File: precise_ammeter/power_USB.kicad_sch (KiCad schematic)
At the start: 21 parts, among them J3 USB4110GFA, J5 XT30_Male, U10 TPS7A2450DBVR, U7 TPS7A2433DBVR, U8 TPS7A2450DBVR, U9 LMC7660

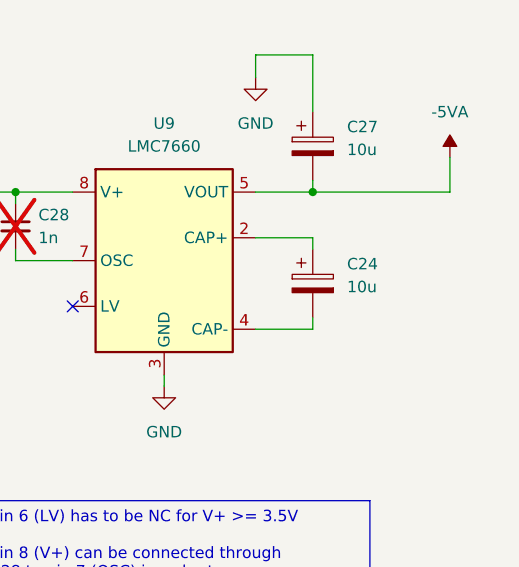
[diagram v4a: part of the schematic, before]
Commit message: adding 1 more 10u cap at voltage inverter
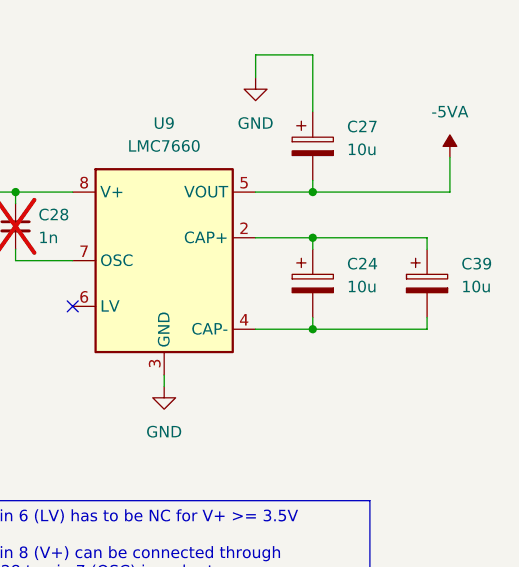
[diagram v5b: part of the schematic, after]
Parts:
- added C39: 10u, Capacitor_SMD:CP_Elec_4x5.4, symbol Device:C_Polarized
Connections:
- net at C24.1, U9.2 (CAP+): now also C39.1
- net at C24.2, U9.4 (CAP-): now also C39.2
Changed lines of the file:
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@@
 	)
 	(junction
+		(at 257.81 115.57)
+		(diameter 0)
+		(color 0 0 0 0)
+	)
+	(junction
 		(at 81.28 127)
 		(diameter 0)
@@
 	)
 	(junction
+		(at 257.81 125.73)
+		(diameter 0)
+		(color 0 0 0 0)
+	)
+	(junction
 		(at 100.33 181.61)
 		(diameter 0)
@@
 	(wire
 		(pts
+			(xy 270.51 115.57) (xy 257.81 115.57)
+		)
+		(stroke
+			(width 0)
+			(type default)
+		)
+	)
+	(wire
+		(pts
 			(xy 85.09 114.3) (xy 81.28 114.3)
 		)
@@
 	(wire
 		(pts
+			(xy 270.51 116.84) (xy 270.51 115.57)
+		)
+		(stroke
+			(width 0)
+			(type default)
+		)
+	)
+	(wire
+		(pts
 			(xy 210.82 46.99) (xy 207.01 46.99)
 		)
@@
 	(wire
 		(pts
-			(xy 194.31 40.64) (xy 194.31 44.45)
+			(xy 257.81 115.57) (xy 257.81 116.84)
 		)
 		(stroke
@@
 	(wire
 		(pts
-			(xy 110.49 116.84) (xy 110.49 119.38)
+			(xy 194.31 40.64) (xy 194.31 44.45)
 		)
 		(stroke
@@
 	(wire
 		(pts
-			(xy 163.83 110.49) (xy 167.64 110.49)
+			(xy 110.49 116.84) (xy 110.49 119.38)
 		)
 		(stroke
@@
 	(wire
 		(pts
-			(xy 251.46 115.57) (xy 257.81 115.57)
+			(xy 163.83 110.49) (xy 167.64 110.49)
 		)
 		(stroke
@@
 	(wire
 		(pts
-			(xy 81.28 45.72) (xy 85.09 45.72)
+			(xy 251.46 115.57) (xy 257.81 115.57)
 		)
 		(stroke
@@
 	(wire
 		(pts
-			(xy 106.68 55.88) (xy 114.3 55.88)
+			(xy 81.28 45.72) (xy 85.09 45.72)
 		)
 		(stroke
@@
 	(wire
 		(pts
-			(xy 257.81 124.46) (xy 257.81 125.73)
+			(xy 106.68 55.88) (xy 114.3 55.88)
 		)
 		(stroke
@@
 	(wire
 		(pts
-			(xy 257.81 115.57) (xy 257.81 116.84)
+			(xy 257.81 124.46) (xy 257.81 125.73)
 		)
 		(stroke
@@
 	(wire
 		(pts
+			(xy 270.51 124.46) (xy 270.51 125.73)
+		)
+		(stroke
+			(width 0)
+			(type default)
+		)
+	)
+	(wire
+		(pts
 			(xy 81.28 116.84) (xy 81.28 121.92)
 		)
@@
 	(wire
 		(pts
+			(xy 257.81 125.73) (xy 270.51 125.73)
+		)
+		(stroke
+			(width 0)
+			(type default)
+		)
+	)
+	(wire
+		(pts
 			(xy 60.96 181.61) (xy 60.96 176.53)
 		)
@@
 					(unit 1)
 				)
+			)
+		)
+	)
+	(symbol
+		(lib_id "Device:C_Polarized")
+		(at 270.51 120.65 0)
+		(unit 1)
+		(exclude_from_sim no)
+		(in_bom yes)
+		(on_board yes)
+		(dnp no)
+		(fields_autoplaced yes)
+		(property "Reference" "C39"
+			(at 274.32 118.4909 0)
+			(effects
+				(font
+					(size 1.27 1.27)
+				)
+				(justify left)
+			)
+		)
+		(property "Value" "10u"
+			(at 274.32 121.0309 0)
+			(effects
+				(font
+					(size 1.27 1.27)
+				)
+				(justify left)
+			)
+		)
+		(property "Footprint" "Capacitor_SMD:CP_Elec_4x5.4"
+			(at 271.4752 124.46 0)
+			(effects
+				(font
+					(size 1.27 1.27)
+				)
+				(hide yes)
+			)
+		)
+		(property "Datasheet" "~"
+			(at 270.51 120.65 0)
+			(effects
+				(font
+					(size 1.27 1.27)
+				)
+				(hide yes)
+			)
+		)
+		(property "Description" "Polarized capacitor"
+			(at 270.51 120.65 0)
+			(effects
+				(font
+					(size 1.27 1.27)
+				)
+				(hide yes)
+			)
+		)
+		(property "Product link" "EDH106M025S9BAA"
+			(at 270.51 120.65 0)
+			(effects
+				(font
+					(size 1.27 1.27)
+				)
+				(hide yes)
+			)
+		)
+		(pin "2"
+		)
+		(pin "1"
+		)
+		(instances
+			(project "precise_ammeter"
+				(path "/7da3b652-85ac-4caa-8d8d-9cad461e9c85/9e6d6147-95e6-4ef0-a238-5628802dd2a2"
+					(reference "C39")
+					(unit 1)
+				)

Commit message: added step model for xt30
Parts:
- J5: footprint Connector_AMASS:AMASS_XT30UPB-M_1x02_P5.0mm_Vertical -> xt30:AMASS_XT30UPB-M_1x02_P5.0mm_Vertical
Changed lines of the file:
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@@
 			)
 		)
-		(property "Footprint" "Connector_AMASS:AMASS_XT30UPB-M_1x02_P5.0mm_Vertical"
+		(property "Footprint" "xt30:AMASS_XT30UPB-M_1x02_P5.0mm_Vertical"
 			(at 33.02 64.77 0)
 			(effects

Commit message: layout started
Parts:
- U10, U8: footprint TPS7A2450DBVR:SOT_50DBVR -> TPS7A2433DBVR:SOT23_DBV_TEX
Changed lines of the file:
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@@
 			)
 		)
-		(property "Footprint" "TPS7A2450DBVR:SOT_50DBVR"
+		(property "Footprint" "TPS7A2433DBVR:SOT23_DBV_TEX"
 			(at 194.818 97.536 0)
 			(effects
@@
 			)
 		)
-		(property "Footprint" "TPS7A2450DBVR:SOT_50DBVR"
+		(property "Footprint" "TPS7A2433DBVR:SOT23_DBV_TEX"
 			(at 225.298 31.496 0)
 			(effects

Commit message: placement finished
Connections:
- net GND: now also J5.1 (Pin_1); no longer J5.2 (Pin_2)
- net VBUS: now also J5.2 (Pin_2); no longer J5.1 (Pin_1)
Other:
- moved on the sheet: J5
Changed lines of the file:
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@@
 	(wire
 		(pts
+			(xy 38.1 71.12) (xy 31.75 71.12)
+		)
+		(stroke
+			(width 0)
+			(type default)
+		)
+	)
+	(wire
+		(pts
 			(xy 257.81 110.49) (xy 273.05 110.49)
 		)
@@
 	(wire
 		(pts
-			(xy 38.1 67.31) (xy 41.91 67.31)
+			(xy 106.68 57.15) (xy 106.68 55.88)
 		)
 		(stroke
@@
 	(wire
 		(pts
-			(xy 106.68 57.15) (xy 106.68 55.88)
+			(xy 232.41 55.88) (xy 232.41 54.61)
 		)
 		(stroke
@@
 	(wire
 		(pts
-			(xy 232.41 55.88) (xy 232.41 54.61)
+			(xy 110.49 121.92) (xy 130.81 121.92)
 		)
 		(stroke
@@
 	(wire
 		(pts
-			(xy 110.49 121.92) (xy 130.81 121.92)
+			(xy 60.96 181.61) (xy 64.77 181.61)
 		)
 		(stroke
@@
 	(wire
 		(pts
-			(xy 60.96 181.61) (xy 64.77 181.61)
+			(xy 114.3 45.72) (xy 114.3 46.99)
 		)
 		(stroke
@@
 	(wire
 		(pts
-			(xy 114.3 45.72) (xy 114.3 46.99)
+			(xy 167.64 111.76) (xy 167.64 110.49)
 		)
 		(stroke
@@
 	(wire
 		(pts
-			(xy 167.64 111.76) (xy 167.64 110.49)
+			(xy 224.79 118.11) (xy 224.79 116.84)
 		)
 		(stroke
@@
 	(wire
 		(pts
-			(xy 41.91 64.77) (xy 41.91 62.23)
+			(xy 257.81 115.57) (xy 257.81 116.84)
 		)
 		(stroke
@@
 	(wire
 		(pts
-			(xy 224.79 118.11) (xy 224.79 116.84)
+			(xy 194.31 40.64) (xy 194.31 44.45)
 		)
 		(stroke
@@
 	(wire
 		(pts
-			(xy 257.81 115.57) (xy 257.81 116.84)
+			(xy 110.49 116.84) (xy 110.49 119.38)
 		)
 		(stroke
@@
 	(wire
 		(pts
-			(xy 194.31 40.64) (xy 194.31 44.45)
+			(xy 163.83 110.49) (xy 167.64 110.49)
 		)
 		(stroke
@@
 	(wire
 		(pts
-			(xy 110.49 116.84) (xy 110.49 119.38)
+			(xy 38.1 68.58) (xy 31.75 68.58)
 		)
 		(stroke
@@
 	(wire
 		(pts
-			(xy 163.83 110.49) (xy 167.64 110.49)
+			(xy 251.46 115.57) (xy 257.81 115.57)
 		)
 		(stroke
@@
 	(wire
 		(pts
-			(xy 251.46 115.57) (xy 257.81 115.57)
+			(xy 31.75 71.12) (xy 31.75 73.66)
 		)
 		(stroke
@@
 	(wire
 		(pts
-			(xy 81.28 121.92) (xy 85.09 121.92)
+			(xy 31.75 68.58) (xy 31.75 66.04)
 		)
 		(stroke
@@
 	(wire
 		(pts
-			(xy 194.31 44.45) (xy 198.12 44.45)
+			(xy 81.28 121.92) (xy 85.09 121.92)
 		)
 		(stroke
@@
 	(wire
 		(pts
-			(xy 85.09 129.54) (xy 81.28 129.54)
+			(xy 194.31 44.45) (xy 198.12 44.45)
 		)
 		(stroke
@@
 	(wire
 		(pts
-			(xy 105.41 45.72) (xy 114.3 45.72)
+			(xy 85.09 129.54) (xy 81.28 129.54)
 		)
 		(stroke
@@
 	(wire
 		(pts
-			(xy 38.1 64.77) (xy 41.91 64.77)
+			(xy 105.41 45.72) (xy 114.3 45.72)
 		)
 		(stroke
@@
 	(wire
 		(pts
-			(xy 41.91 67.31) (xy 41.91 69.85)
-		)
-		(stroke
-			(width 0)
-			(type default)
-		)
-	)
-	(wire
-		(pts
 			(xy 257.81 110.49) (xy 257.81 109.22)
 		)
@@
 	(symbol
 		(lib_id "power:VBUS")
-		(at 41.91 62.23 0)
+		(at 31.75 66.04 0)
 		(unit 1)
 		(exclude_from_sim no)
@@
 		(fields_autoplaced yes)
 		(property "Reference" "#PWR076"
-			(at 41.91 66.04 0)
+			(at 31.75 69.85 0)
 			(effects
 				(font
@@
 		)
 		(property "Value" "VBUS"
-			(at 41.91 57.15 0)
+			(at 31.75 60.96 0)
 			(effects
 				(font
@@
 		)
 		(property "Footprint" ""
-			(at 41.91 62.23 0)
+			(at 31.75 66.04 0)
 			(effects
 				(font
@@
 		)
 		(property "Datasheet" ""
-			(at 41.91 62.23 0)
+			(at 31.75 66.04 0)
 			(effects
 				(font
@@
 		)
 		(property "Description" "Power symbol creates a global label with name \"VBUS\""
-			(at 41.91 62.23 0)
+			(at 31.75 66.04 0)
 			(effects
 				(font
@@
 	)
 	(symbol
-		(lib_id "power:GND")
-		(at 41.91 69.85 0)
-		(unit 1)
-		(exclude_from_sim no)
-		(in_bom yes)
-		(on_board yes)
-		(dnp no)
-		(fields_autoplaced yes)
-		(property "Reference" "#PWR077"
-			(at 41.91 76.2 0)
-			(effects
-				(font
-					(size 1.27 1.27)
-				)
-				(hide yes)
-			)
-		)
-		(property "Value" "GND"
-			(at 41.91 74.93 0)
-			(effects
-				(font
-					(size 1.27 1.27)
-				)
-			)
-		)
-		(property "Footprint" ""
-			(at 41.91 69.85 0)
-			(effects
-				(font
-					(size 1.27 1.27)
-				)
-				(hide yes)
-			)
-		)
-		(property "Datasheet" ""
-			(at 41.91 69.85 0)
-			(effects
-				(font
-					(size 1.27 1.27)
-				)
-				(hide yes)
-			)
-		)
-		(property "Description" "Power symbol creates a global label with name \"GND\" , ground"
-			(at 41.91 69.85 0)
-			(effects
-				(font
-					(size 1.27 1.27)
-				)
-				(hide yes)
-			)
-		)
-		(pin "1"
-		)
-		(instances
-			(project "precise_ammeter"
-				(path "/7da3b652-85ac-4caa-8d8d-9cad461e9c85/9e6d6147-95e6-4ef0-a238-5628802dd2a2"
-					(reference "#PWR077")
-					(unit 1)
-				)
-			)
-		)
-	)
-	(symbol
 		(lib_id "power:+3V3")
 		(at 118.11 41.91 0)
@@
 	(symbol
 		(lib_id "power:GND")
+		(at 31.75 73.66 0)
+		(unit 1)
+		(exclude_from_sim no)
+		(in_bom yes)
+		(on_board yes)
+		(dnp no)
+		(fields_autoplaced yes)
+		(property "Reference" "#PWR077"
+			(at 31.75 80.01 0)
+			(effects
+				(font
+					(size 1.27 1.27)
+				)
+				(hide yes)
+			)
+		)
+		(property "Value" "GND"
+			(at 31.75 78.74 0)
+			(effects
+				(font
+					(size 1.27 1.27)
+				)
+			)
+		)
+		(property "Footprint" ""
+			(at 31.75 73.66 0)
+			(effects
+				(font
+					(size 1.27 1.27)
+				)
+				(hide yes)
+			)
+		)
+		(property "Datasheet" ""
+			(at 31.75 73.66 0)
+			(effects
+				(font
+					(size 1.27 1.27)
+				)
+				(hide yes)
+			)
+		)
+		(property "Description" "Power symbol creates a global label with name \"GND\" , ground"
+			(at 31.75 73.66 0)
+			(effects
+				(font
+					(size 1.27 1.27)
+				)
+				(hide yes)
+			)
+		)
+		(pin "1"
+		)
+		(instances
+			(project "precise_ammeter"
+				(path "/7da3b652-85ac-4caa-8d8d-9cad461e9c85/9e6d6147-95e6-4ef0-a238-5628802dd2a2"
+					(reference "#PWR077")
+					(unit 1)
+				)
+			)
+		)
+	)
+	(symbol
+		(lib_id "power:GND")
 		(at 201.93 121.92 0)
 		(unit 1)
@@
 	(symbol
 		(lib_id "Connector:Conn_01x02_Pin")
-		(at 33.02 64.77 0)
+		(at 43.18 71.12 180)
 		(unit 1)
 		(exclude_from_sim no)
@@
 		(dnp no)
 		(property "Reference" "J5"
-			(at 33.02 61.976 0)
+			(at 43.18 73.914 0)
 			(effects
 				(font
@@
 		)
 		(property "Value" "XT30_Male"
-			(at 34.29 69.85 0)
+			(at 41.91 66.04 0)
 			(effects
 				(font
@@
 		)
 		(property "Footprint" "xt30:AMASS_XT30UPB-M_1x02_P5.0mm_Vertical"
-			(at 33.02 64.77 0)
+			(at 43.18 71.12 0)
 			(effects
 				(font
@@
 		)
 		(property "Datasheet" "~"
-			(at 33.02 64.77 0)
+			(at 43.18 71.12 0)
 			(effects
 				(font
@@
 		)
 		(property "Description" "Generic connector, single row, 01x02, script generated"
-			(at 33.02 64.77 0)
+			(at 43.18 71.12 0)
 			(effects
 				(font
